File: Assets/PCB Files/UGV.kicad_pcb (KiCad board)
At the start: 2 copper layers, 134 x 155.5 mm, 76 parts, among them J13 USB3_A, J15 Screw_Terminal_01x12, J16 Screw_Terminal_01x12, J17 Screw_Terminal_01x12, J18 Screw_Terminal_01x12, U1 INA219AxDCN, U2 LMR33630ADDA, U3 SN74LVC8T245, U4 Teensy4.1, U5 SN74LVC8T245

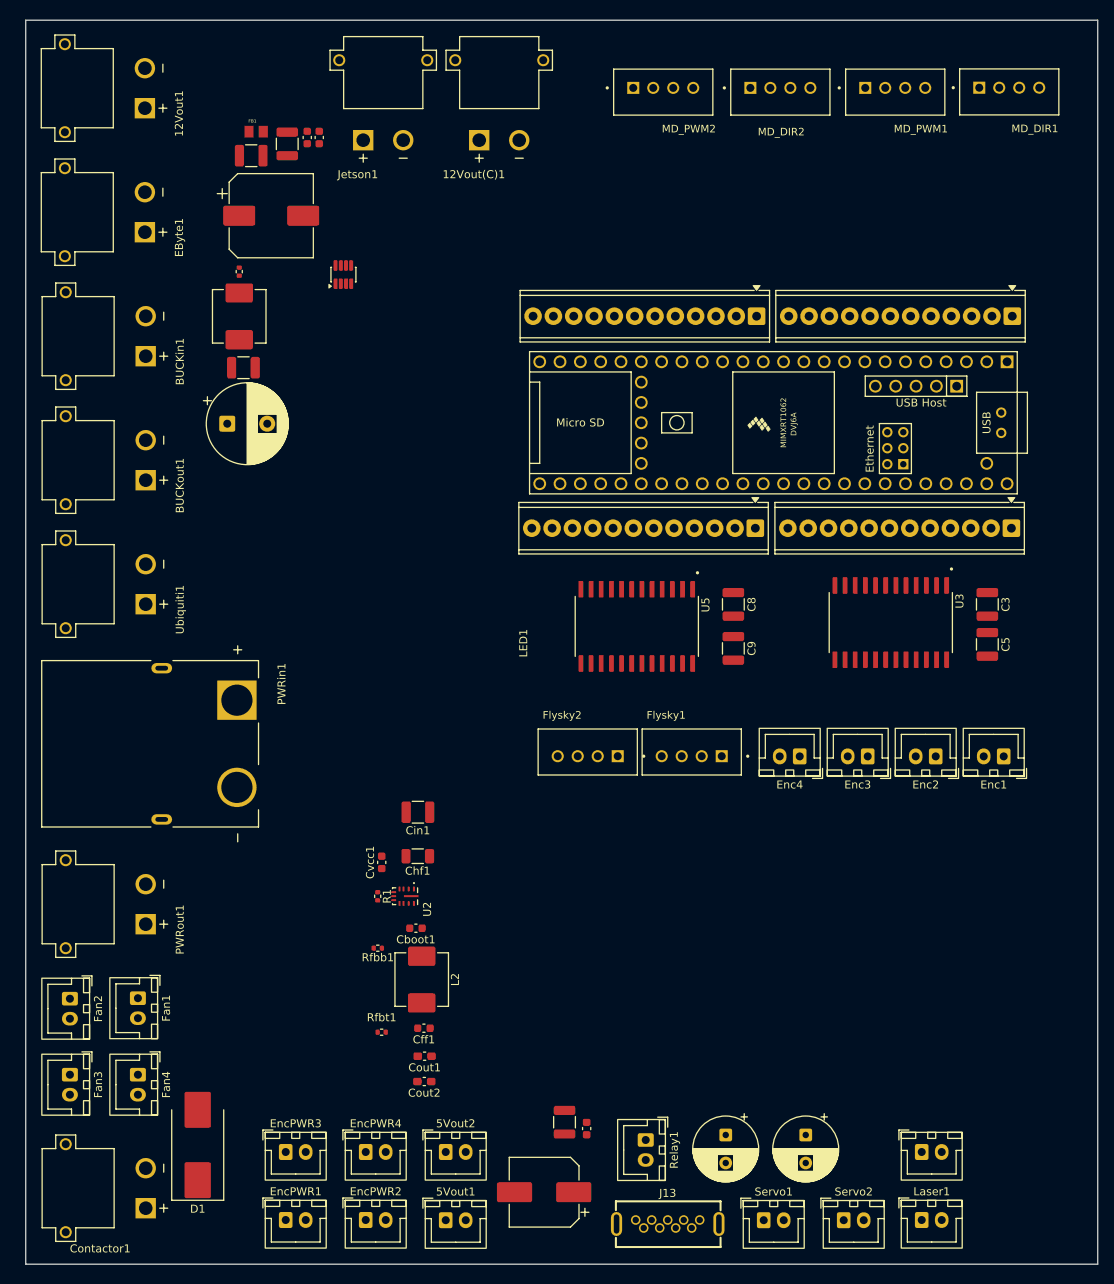
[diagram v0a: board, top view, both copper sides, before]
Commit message: Added Logo and edited layout
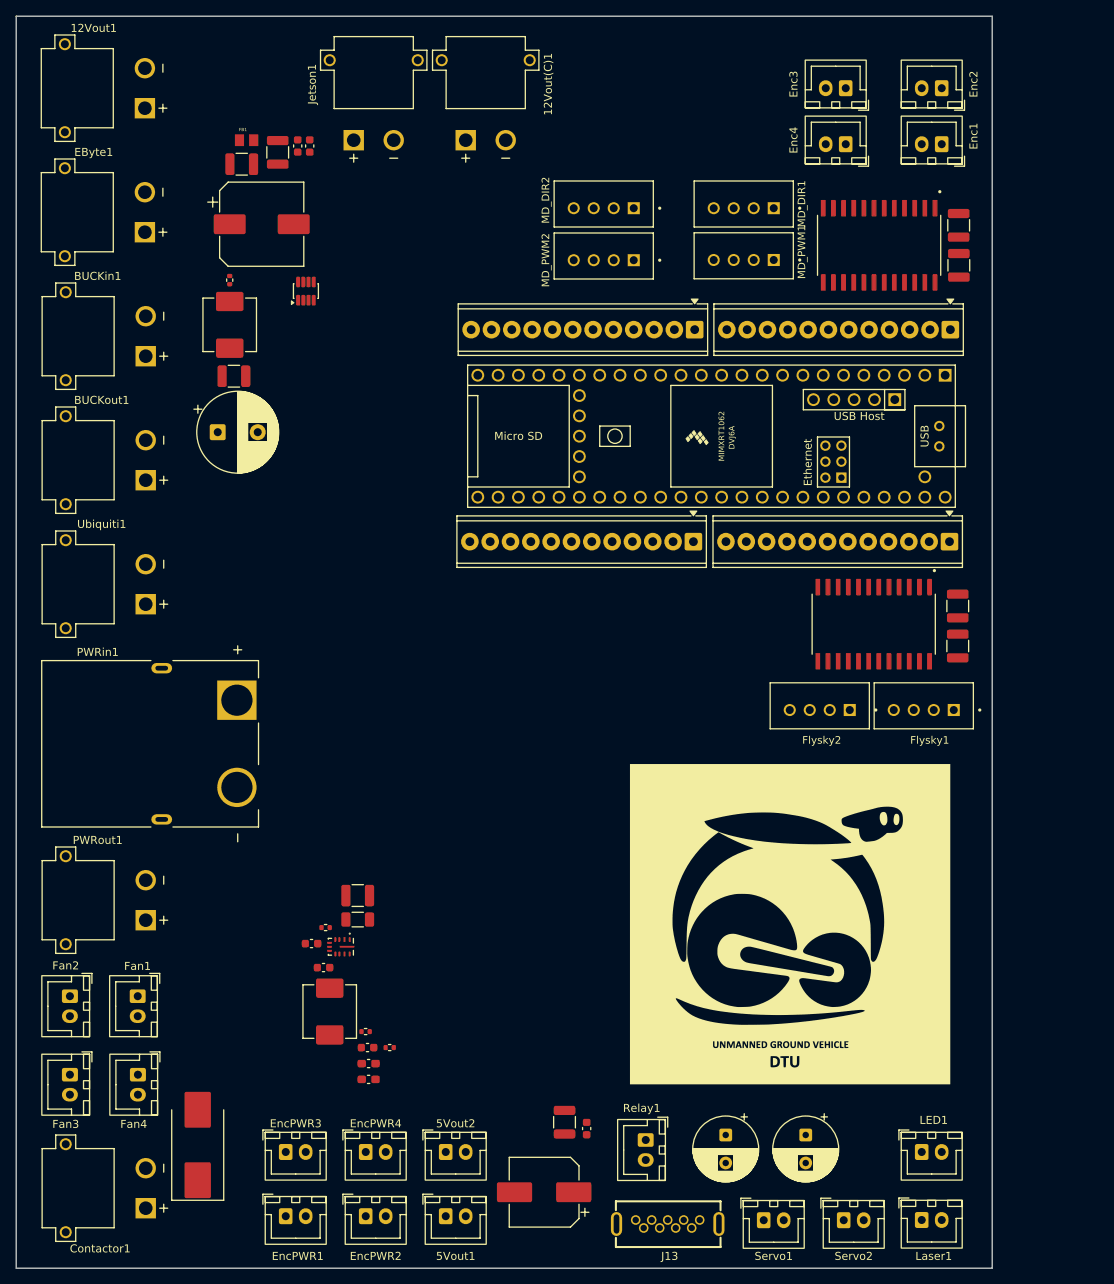
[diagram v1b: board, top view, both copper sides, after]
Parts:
- added G***: LOGO, logofoot.preety:logonew, F.Cu at (96.6, 114.5)
- L2: value 3.3uH -> 10uH
- moved Enc3 83.6 mm to (103.5, 10.0)
- moved Enc2 83.5 mm to (115.5, 10.0)
- moved Enc1 76.9 mm to (115.5, 17.0)
- moved Enc4 76.7 mm to (103.5, 17.0)
- moved C5 52.5 mm to (117.6, 27.1), turned to 90 degrees
- moved U3 47.2 mm to (107.7, 29.6)
- moved C3 42.5 mm to (117.6, 32.1)
- moved MD_DIR1 36.0 mm to (90.8, 24.5), turned to 0 degrees
- moved U5 29.6 mm to (107.0, 77.0)
- moved Flysky1 29.6 mm to (113.3, 87.2)
- moved Flysky2 29.6 mm to (100.3, 87.2)
- moved C9 28.1 mm to (117.5, 79.7)
- moved C8 28.1 mm to (117.5, 74.7)
- moved MD_PWM1 27.9 mm to (90.8, 30.9), turned to 0 degrees
- moved MD_DIR2 26.1 mm to (73.2, 24.5), turned to 0 degrees
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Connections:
- C3 pad 2: /Vin -> Net-(C3-Pad2)
- C5 pad 2: /3V3 -> Net-(U3-V_{CCA})
- C8 pad 2: /3V3 -> Net-(U5-V_{CCA})
- C9 pad 2: /Vin -> Net-(C9-Pad2)
- Enc1 pad 1: Net-(U3-B1) -> unconnected-(Enc1-Pad1)
- Enc1 pad 2: Net-(U3-B2) -> unconnected-(Enc1-Pad2)
- Enc2 pad 1: Net-(U3-B3) -> unconnected-(Enc2-Pad1)
- Enc2 pad 2: Net-(U3-B4) -> unconnected-(Enc2-Pad2)
- Enc3 pad 1: Net-(U3-B5) -> unconnected-(Enc3-Pad1)
- Enc3 pad 2: Net-(U3-B6) -> unconnected-(Enc3-Pad2)
- Enc4 pad 1: Net-(U3-B7) -> unconnected-(Enc4-Pad1)
- Enc4 pad 2: Net-(U3-B8) -> unconnected-(Enc4-Pad2)
- Flysky1 pad 1: Net-(U5-B1) -> unconnected-(Flysky1-Pad1)
- Flysky1 pad 2: Net-(U5-B2) -> unconnected-(Flysky1-Pad2)
- Flysky1 pad 3: Net-(U5-B3) -> unconnected-(Flysky1-Pad3)
- Flysky1 pad 4: Net-(U5-B4) -> unconnected-(Flysky1-Pad4)
- Flysky2 pad 1: Net-(U5-B5) -> unconnected-(Flysky2-Pad1)
- Flysky2 pad 2: Net-(U5-B6) -> unconnected-(Flysky2-Pad2)
- Flysky2 pad 3: Net-(U5-B7) -> unconnected-(Flysky2-Pad3)
- Flysky2 pad 4: Net-(U5-B8) -> unconnected-(Flysky2-Pad4)
- U3 pad 1: /3V3 -> Net-(U3-V_{CCA})
- U3 pad 14: Net-(U3-B8) -> unconnected-(U3-B8-Pad14)
- U3 pad 15: Net-(U3-B7) -> unconnected-(U3-B7-Pad15)
- U3 pad 16: Net-(U3-B6) -> unconnected-(U3-B6-Pad16)
- U3 pad 17: Net-(U3-B5) -> unconnected-(U3-B5-Pad17)
- U3 pad 18: Net-(U3-B4) -> unconnected-(U3-B4-Pad18)
- U3 pad 19: Net-(U3-B3) -> unconnected-(U3-B3-Pad19)
- U3 pad 20: Net-(U3-B2) -> unconnected-(U3-B2-Pad20)
- U3 pad 21: Net-(U3-B1) -> unconnected-(U3-B1-Pad21)
- U3 pad 23: /Vin -> Net-(C3-Pad2)
- U3 pad 24: /Vin -> Net-(C3-Pad2)
- U5 pad 1: /3V3 -> Net-(U5-V_{CCA})
- U5 pad 14: Net-(U5-B8) -> unconnected-(U5-B8-Pad14)
- U5 pad 15: Net-(U5-B7) -> unconnected-(U5-B7-Pad15)
- U5 pad 16: Net-(U5-B6) -> unconnected-(U5-B6-Pad16)
- U5 pad 17: Net-(U5-B5) -> unconnected-(U5-B5-Pad17)
- U5 pad 18: Net-(U5-B4) -> unconnected-(U5-B4-Pad18)
- U5 pad 19: Net-(U5-B3) -> unconnected-(U5-B3-Pad19)
- U5 pad 20: Net-(U5-B2) -> unconnected-(U5-B2-Pad20)
- U5 pad 21: Net-(U5-B1) -> unconnected-(U5-B1-Pad21)
- U5 pad 23: /Vin -> Net-(C9-Pad2)
- U5 pad 24: /Vin -> Net-(C9-Pad2)
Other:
- board size 134 x 155.5 mm -> 122 x 156.5 mm
